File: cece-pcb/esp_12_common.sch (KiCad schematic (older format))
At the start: 15 parts, among them SW201 RES, U201 ESP-12F

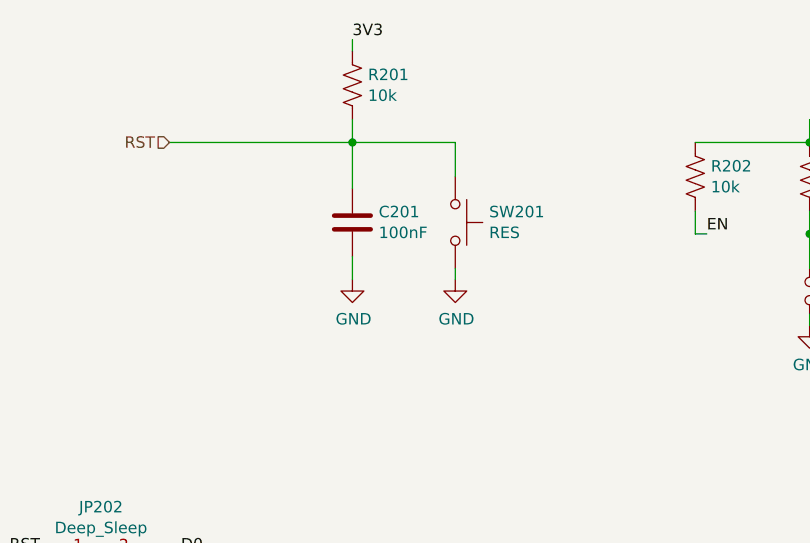
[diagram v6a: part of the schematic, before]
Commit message: Add resistor to limit peak current in the reset pushbutton. Prevents contact welding
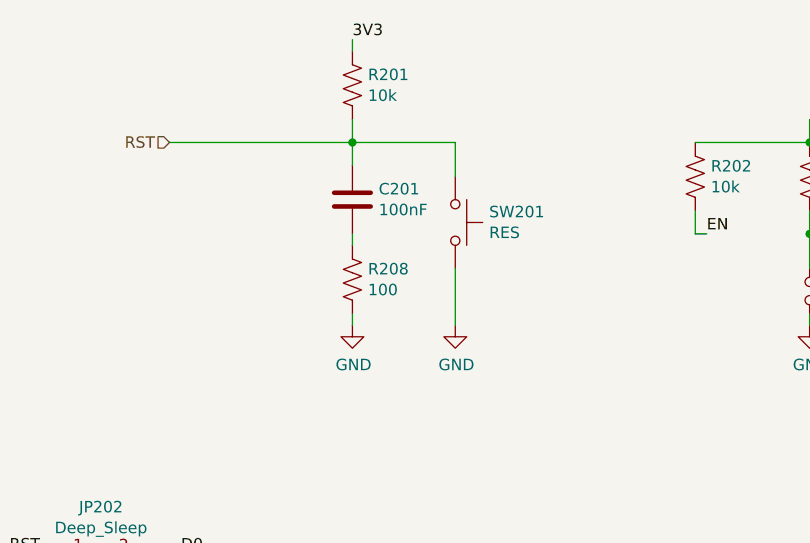
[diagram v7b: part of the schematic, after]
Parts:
- added R208: 100, Resistor_THT:R_Axial_DIN0207_L6.3mm_D2.5mm_P7.62mm_Horizontal, symbol Device:R_US
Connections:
- net GND: now also R208.2; no longer C201.2
- new net: C201.2, R208.1
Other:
- moved on the sheet: C201
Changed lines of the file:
@@
 L Device:C C201
 U 1 1 5FC2FA50
-P 3000 1850
-F 0 "C201" H 3115 1896 50  0000 L CNN
-F 1 "100nF" H 3115 1805 50  0000 L CNN
-F 2 "Capacitor_THT:C_Disc_D4.3mm_W1.9mm_P5.00mm" H 3038 1700 50  0001 C CNN
-F 3 "~" H 3000 1850 50  0001 C CNN
-	1    3000 1850
-	1    0    0    -1
-$EndComp
-Wire Wire Line
-	3000 1500 3000 1700
+P 3000 1750
+F 0 "C201" H 3115 1796 50  0000 L CNN
+F 1 "100nF" H 3115 1705 50  0000 L CNN
+F 2 "Capacitor_THT:C_Disc_D4.3mm_W1.9mm_P5.00mm" H 3038 1600 50  0001 C CNN
+F 3 "~" H 3000 1750 50  0001 C CNN
+	1    3000 1750
+	1    0    0    -1
+$EndComp
+Wire Wire Line
+	3000 1500 3000 1600
 $Comp
 L power:GND #PWR0201
 U 1 1 5FC307D2
-P 3000 2100
-F 0 "#PWR0201" H 3000 1850 50  0001 C CNN
-F 1 "GND" H 3005 1927 50  0000 C CNN
-F 2 "" H 3000 2100 50  0001 C CNN
-F 3 "" H 3000 2100 50  0001 C CNN
-	1    3000 2100
-	1    0    0    -1
-$EndComp
-Wire Wire Line
-	3000 2100 3000 2000
+P 3000 2300
+F 0 "#PWR0201" H 3000 2050 50  0001 C CNN
+F 1 "GND" H 3005 2127 50  0000 C CNN
+F 2 "" H 3000 2300 50  0001 C CNN
+F 3 "" H 3000 2300 50  0001 C CNN
+	1    3000 2300
+	1    0    0    -1
+$EndComp
 Text Notes 3250 6700 0    50   ~ 0
 https://escapequotes.net/wp-content/uploads/2016/02/wemos-d1-mini-shematics.jpg
@@
 L power:GND #PWR0202
 U 1 1 5FD63E00
-P 3450 2100
-F 0 "#PWR0202" H 3450 1850 50  0001 C CNN
-F 1 "GND" H 3455 1927 50  0000 C CNN
-F 2 "" H 3450 2100 50  0001 C CNN
-F 3 "" H 3450 2100 50  0001 C CNN
-	1    3450 2100
-	1    0    0    -1
-$EndComp
-Wire Wire Line
-	3450 2050 3450 2100
+P 3450 2300
+F 0 "#PWR0202" H 3450 2050 50  0001 C CNN
+F 1 "GND" H 3455 2127 50  0000 C CNN
+F 2 "" H 3450 2300 50  0001 C CNN
+F 3 "" H 3450 2300 50  0001 C CNN
+	1    3450 2300
+	1    0    0    -1
+$EndComp
+Wire Wire Line
+	3450 2050 3450 2300
 Text HLabel 6700 4950 3    50   BiDi ~ 0
 GND
@@
 Wire Wire Line
 	6950 4200 7350 4200
+$Comp
+L Device:R_US R208
+U 1 1 6034B30A
+P 3000 2100
+F 0 "R208" H 3068 2146 50  0000 L CNN
+F 1 "100" H 3068 2055 50  0000 L CNN
+F 2 "Resistor_THT:R_Axial_DIN0207_L6.3mm_D2.5mm_P7.62mm_Horizontal" V 3040 2090 50  0001 C CNN
+F 3 "~" H 3000 2100 50  0001 C CNN
+	1    3000 2100
+	1    0    0    -1
+$EndComp
+Wire Wire Line
+	3000 2300 3000 2250
+Wire Wire Line
+	3000 1950 3000 1900
 $EndSCHEMATC
